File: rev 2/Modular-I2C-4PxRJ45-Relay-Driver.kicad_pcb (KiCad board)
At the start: 2 copper layers, 69.5 x 100 mm, 123 parts, among them J1 Conn_02x03_Odd_Even, J2 Conn_02x03_Odd_Even, J3 Screw_Terminal_01x02, J4 Screw_Terminal_01x02, Q51 2N7002, Q52 2N7002, Q53 2N7002, Q54 2N7002, Q55 2N7002, Q56 2N7002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

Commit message: logo
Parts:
- added G***: LOGO, Vizista_Logo:Vizista-Logo-Text-10mm, F.Cu at (162.7, 34.7)
- added G***: LOGO, Vizista_Logo:Vizista-Logo-Text-20mm, B.Cu at (166.5, 38.5)
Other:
- board text added: "Based on design by Jon Oxer by Austin's Creations"

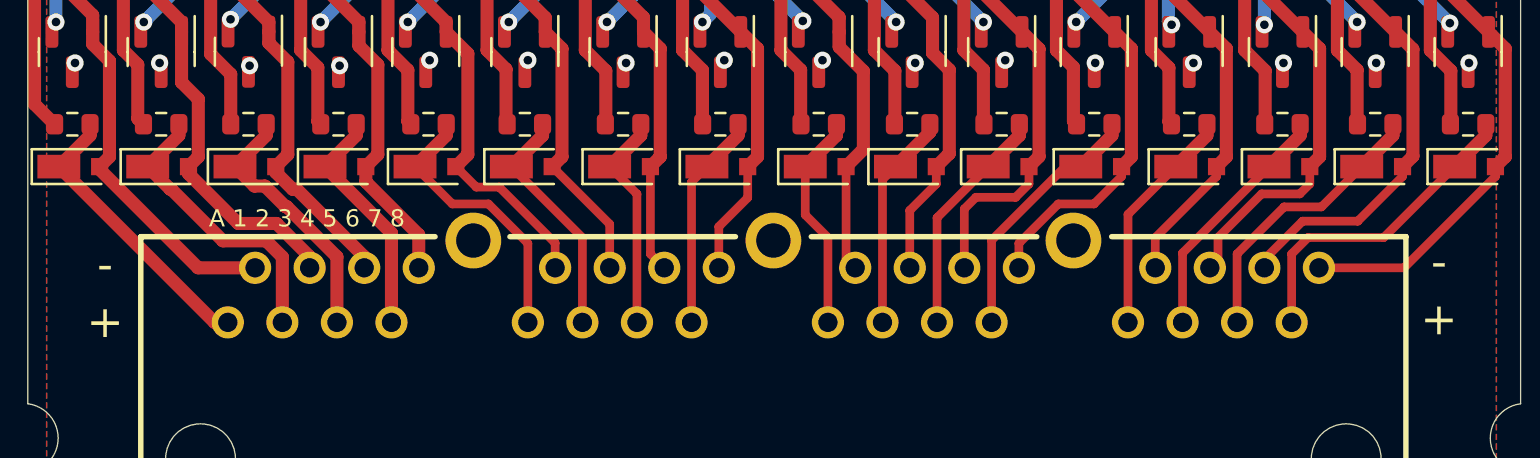
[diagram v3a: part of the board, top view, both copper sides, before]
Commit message: RJ45 to Pluggable break out
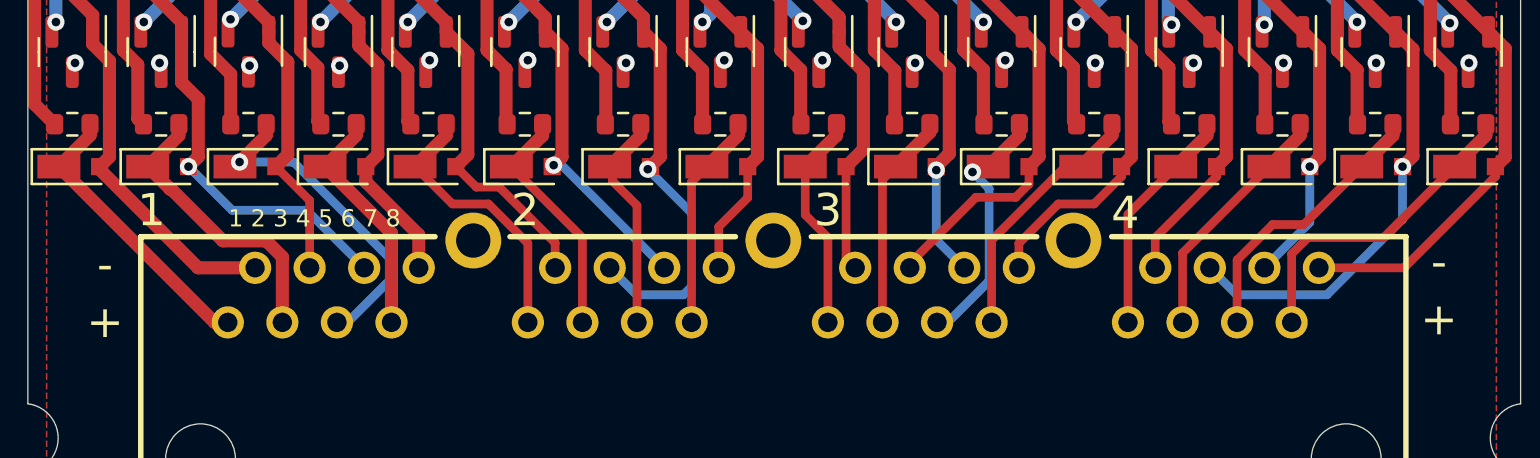
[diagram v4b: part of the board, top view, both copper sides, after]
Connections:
- RJ45-1 pad A4: RC2- -> RC3-
- RJ45-1 pad A6: RC3- -> RC2-
- RJ45-1 pad B4: RC6- -> RC7-
- RJ45-1 pad B6: RC7- -> RC6-
- RJ45-1 pad C4: RC10- -> RC11-
- RJ45-1 pad C6: RC11- -> RC10-
- RJ45-1 pad D4: RC14- -> RC15-
- RJ45-1 pad D6: RC15- -> RC14-
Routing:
- net RC7-: track 14.9 -> 20.9 mm, vias 0 -> 1
- net RC15-: track 18.9 -> 23.4 mm, vias 0 -> 1
- net RC3+: track 12.1 -> 15.8 mm, vias 0 -> 1
- net RC14-: track 17.6 -> 15.6 mm, vias 0 -> 1
- net RC2-: track 18.1 -> 20.1 mm, vias 0 -> 1
- net RC6-: track 15.8 -> 17.1 mm, vias 0 -> 1
- net RC3-: track 16.6 -> 15.4 mm
- net RC11-: track 17.0 -> 18.1 mm
- net RC11+: track 10.8 -> 11.2 mm, vias 0 -> 1
- net RC10-: track 15.2 -> 15.3 mm, vias 0 -> 1
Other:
- board text added: "1 2 3 4 5 6 7 8"
- board text added: "3"
- board text added: "4"
- board text removed: "A 1 2 3 4 5 6 7 8"

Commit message: cleanup
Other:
- board text removed: "1: Data 1 2: Data 2 3: Data 3 4: VIN 5: VIN 6: Data 4 7: GND 8: GND"
- board text removed: "Based on design by Jon Oxer by Austin's Creations modified by Mattar"
- board text removed: "Copyright 2019-2021 SuperHouse Automation Pty Ltd Released under the terms of the TAPR Open Hardware License: www.tapr.org/OHL"
- board text removed: "RJ45 Pinout"
- board text removed: "www.superhouse.tv/i2crj45"
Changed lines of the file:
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@@
       ) (layer "B.SilkS") (width 0) (fill solid))
   )
-  (gr_line (start 348.456014 74.534986) (end 348.456014 89.534986) (layer "B.SilkS") (width 0.254))
-  (gr_arc (start 348.456014 89.534986) (mid 347.870233 90.949214) (end 346.456014 91.534986) (layer "B.SilkS") (width 0.254))
-  (gr_arc (start 333.956014 91.534986) (mid 332.541796 90.949204) (end 331.956014 89.534986) (layer "B.SilkS") (width 0.254))
   (gr_line (start 173.688351 56.1308) (end 170.894351 54.3528) (layer "B.SilkS") (width 0.254))
   (gr_line (start 173.180351 55.8768) (end 172.926351 55.8768) (layer "B.SilkS") (width 0.254))
   (gr_line (start 169.116351 55.8768) (end 170.894351 54.6068) (layer "B.SilkS") (width 0.254))
-  (gr_arc (start 346.456014 72.534986) (mid 347.870223 73.120777) (end 348.456014 74.534986) (layer "B.SilkS") (width 0.254))
   (gr_line (start 168.354351 56.1308) (end 173.688351 56.1308) (layer "B.SilkS") (width 0.254))
   (gr_line (start 170.132351 55.3688) (end 171.402351 55.3688) (layer "B.SilkS") (width 0.4064))
   (gr_line (start 170.894351 54.3528) (end 168.354351 56.1308) (layer "B.SilkS") (width 0.254))
   (gr_line (start 171.402351 55.3688) (end 170.894351 55.1148) (layer "B.SilkS") (width 0.4064))
-  (gr_arc (start 331.956014 74.534986) (mid 332.541806 73.120786) (end 333.956014 72.534986) (layer "B.SilkS") (width 0.254))
-  (gr_line (start 346.451014 91.559986) (end 333.951014 91.559986) (layer "B.SilkS") (width 0.254))
   (gr_line (start 172.418351 55.6228) (end 170.894351 54.8608) (layer "B.SilkS") (width 0.4064))
   (gr_line (start 170.894351 54.6068) (end 172.926351 55.8768) (layer "B.SilkS") (width 0.254))
   (gr_line (start 172.926351 55.8768) (end 169.116351 55.8768) (layer "B.SilkS") (width 0.254))
   (gr_line (start 170.894351 54.8608) (end 170.132351 55.3688) (layer "B.SilkS") (width 0.4064))
-  (gr_line (start 333.956014 72.534986) (end 346.456014 72.534986) (layer "B.SilkS") (width 0.254))
   (gr_line (start 169.624351 55.6228) (end 172.418351 55.6228) (layer "B.SilkS") (width 0.4064))
   (gr_arc (start 126.7449 83.8794) (mid 126.598453 84.232953) (end 126.2449 84.3794) (layer "F.SilkS") (width 0.15))
@@
     (effects (font (size 1.5 1.5) (thickness 0.3)) (justify mirror))
   )
-  (gr_text "www.superhouse.tv/i2crj45" (at 341.757 108.585) (layer "B.SilkS")
-    (effects (font (size 1.909 1.909) (thickness 0.391)) (justify bottom mirror))
-  )
   (gr_text "Based on design \n by Jon Oxer\n by Austin's Creations\n" (at 152.4 52.578) (layer "B.SilkS")
     (effects (font (size 1.180592 1.180592) (thickness 0.241808)) (justify left bottom mirror))
-  )
-  (gr_text "Modular\n4-Port\nI2C RJ45\nRelay Driver Breakout" (at 345.44 52.705) (layer "B.SilkS")
-    (effects (font (size 2.324 2) (thickness 0.476)) (justify left bottom mirror))
   )
   (gr_text "VCC" (at 121.567 47.197 270) (layer "B.SilkS")
@@
     (effects (font (size 0.8 0.8) (thickness 0.2)) (justify mirror))
   )
-  (gr_text "1: Data 1\n2: Data 2\n3: Data 3\n4: VIN\n5: VIN\n6: Data 4\n7: GND\n8: GND" (at 344.773014 90.797986) (layer "B.SilkS")
-    (effects (font (size 1.26 1.26) (thickness 0.24)) (justify left bottom mirror))
-  )
   (gr_text "GND" (at 116.967 52.197 270) (layer "B.SilkS")
     (effects (font (size 0.8 0.8) (thickness 0.2)) (justify mirror))
@@
     (effects (font (size 0.8 0.8) (thickness 0.2)) (justify mirror))
   )
-  (gr_text "RJ45 Pinout" (at 344.773014 74.414986) (layer "B.SilkS")
-    (effects (font (size 1.148 1.148) (thickness 0.252)) (justify left bottom mirror))
-  )
   (gr_text "2" (at 142.113 117.983) (layer "B.SilkS")
     (effects (font (size 1.5 1.5) (thickness 0.3)) (justify mirror))
   )
-  (gr_text "Copyright 2019-2021 SuperHouse Automation Pty Ltd\n\nReleased under the terms of the TAPR\nOpen Hardware License: www.tapr.org/OHL" (at 362.458 103.759) (layer "B.SilkS")
-    (effects (font (size 1.0541 1.0541) (thickness 0.2159)) (justify left bottom mirror))
-  )
-  (gr_text "Based on design \n by Jon Oxer\n by Austin's Creations\n modified by Mattar\n" (at 347.345 30.861) (layer "B.SilkS")
-    (effects (font (size 1.180592 1.180592) (thickness 0.241808)) (justify left bottom mirror))
-  )
   (gr_text "SCL" (at 121.667 57.097 270) (layer "B.SilkS")

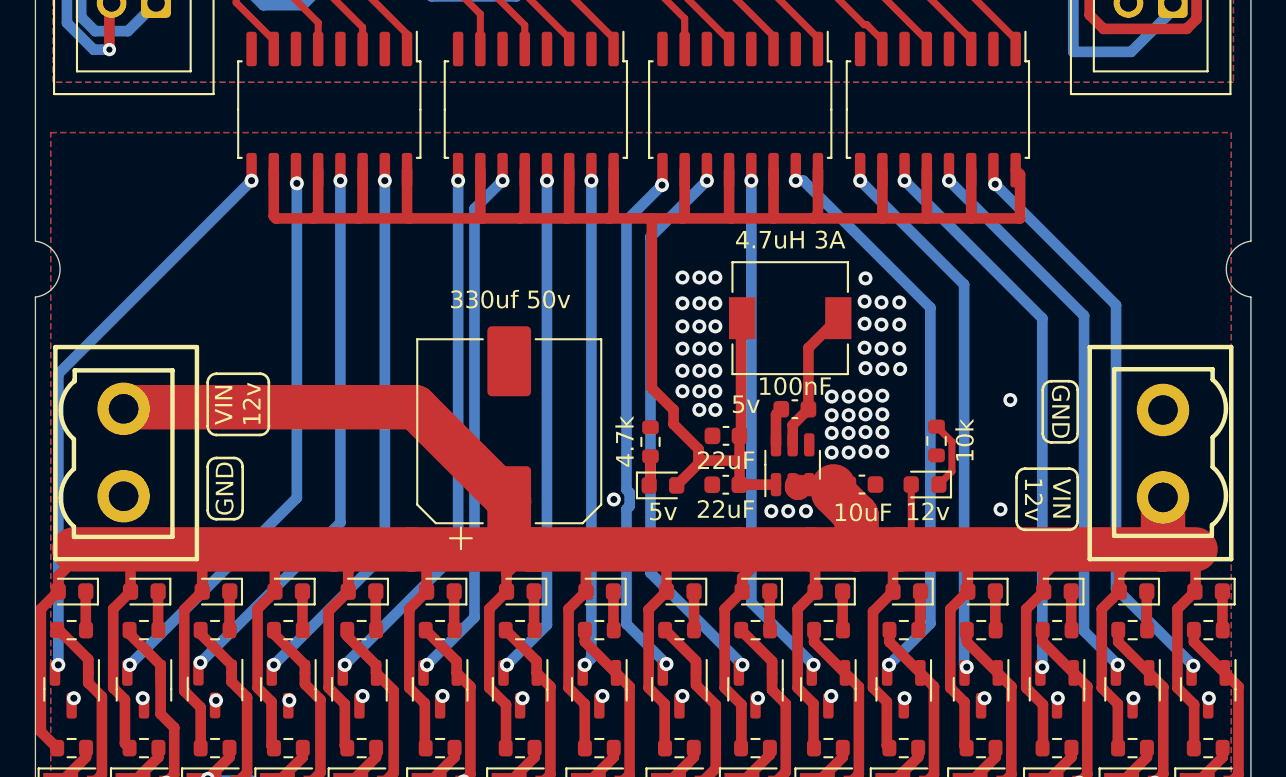
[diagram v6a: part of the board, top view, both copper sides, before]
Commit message: updated to support 5V output for fan speed control in rev2
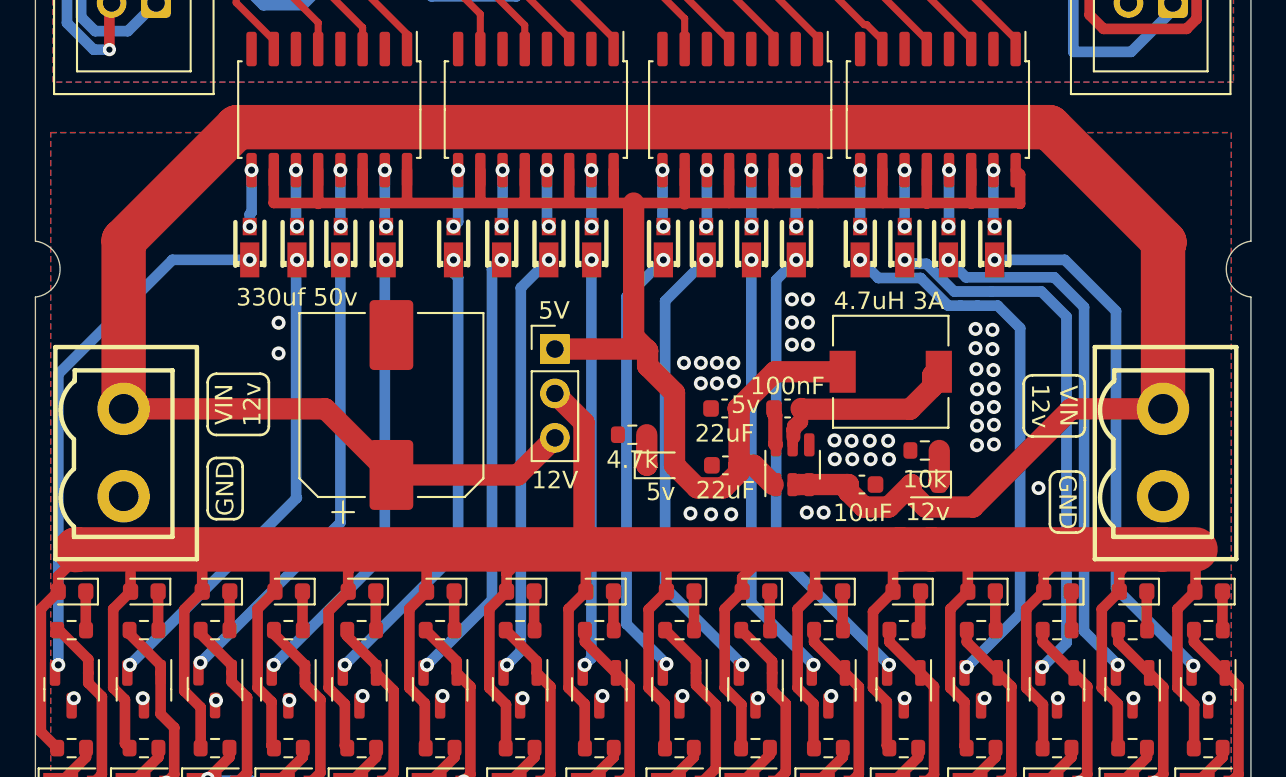
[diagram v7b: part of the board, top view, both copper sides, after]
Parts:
- added D67: 1N4004 SMB, LCSC:LCSC-C94470-MICROSMP_L2.2-W1.3-LS2.5-RD, F.Cu at (134.9, 68.6)
- added D68: 1N4004 SMB, LCSC:LCSC-C94470-MICROSMP_L2.2-W1.3-LS2.5-RD, F.Cu at (132.3, 68.6)
- added D69: 1N4004 SMB, LCSC:LCSC-C94470-MICROSMP_L2.2-W1.3-LS2.5-RD, F.Cu at (129.8, 68.6)
- added D70: 1N4004 SMB, LCSC:LCSC-C94470-MICROSMP_L2.2-W1.3-LS2.5-RD, F.Cu at (127.2, 68.6)
- added D71: 1N4004 SMB, LCSC:LCSC-C94470-MICROSMP_L2.2-W1.3-LS2.5-RD, F.Cu at (138.8, 68.6)
- added D72: 1N4004 SMB, LCSC:LCSC-C94470-MICROSMP_L2.2-W1.3-LS2.5-RD, F.Cu at (141.6, 68.6)
- added D73: 1N4004 SMB, LCSC:LCSC-C94470-MICROSMP_L2.2-W1.3-LS2.5-RD, F.Cu at (144.2, 68.6)
- added D74: 1N4004 SMB, LCSC:LCSC-C94470-MICROSMP_L2.2-W1.3-LS2.5-RD, F.Cu at (146.7, 68.6)
- added D75: 1N4004 SMB, LCSC:LCSC-C94470-MICROSMP_L2.2-W1.3-LS2.5-RD, F.Cu at (150.8, 68.6)
- added D76: 1N4004 SMB, LCSC:LCSC-C94470-MICROSMP_L2.2-W1.3-LS2.5-RD, F.Cu at (153.2, 68.6)
- added D77: 1N4004 SMB, LCSC:LCSC-C94470-MICROSMP_L2.2-W1.3-LS2.5-RD, F.Cu at (155.8, 68.6)
- added D78: 1N4004 SMB, LCSC:LCSC-C94470-MICROSMP_L2.2-W1.3-LS2.5-RD, F.Cu at (158.4, 68.6)
- added D79: 1N4004 SMB, LCSC:LCSC-C94470-MICROSMP_L2.2-W1.3-LS2.5-RD, F.Cu at (162.1, 68.6)
- added D80: 1N4004 SMB, LCSC:LCSC-C94470-MICROSMP_L2.2-W1.3-LS2.5-RD, F.Cu at (164.6, 68.6)
- added D81: 1N4004 SMB, LCSC:LCSC-C94470-MICROSMP_L2.2-W1.3-LS2.5-RD, F.Cu at (167.1, 68.6)
- added D82: 1N4004 SMB, LCSC:LCSC-C94470-MICROSMP_L2.2-W1.3-LS2.5-RD, F.Cu at (169.7, 68.6)
- added JP1: Jumper_3_Open, Connector_PinHeader_2.54mm:PinHeader_1x03_P2.54mm_Vertical, F.Cu at (144.6, 74.7)
- moved C5 6.90 mm to (135.2, 77.8)
- moved L1 6.51 mm to (163.8, 76.0)
- moved C7 1.57 mm to (154.3, 78.0)
- moved D2 1.16 mm to (150.7, 81.3)
- moved R1 1.12 mm to (149.0, 79.5), turned to 0 degrees
- moved C8 1.11 mm to (154.3, 81.3)
- moved R5 0.86 mm to (165.8, 80.5), turned to 180 degrees
- moved C6 0.42 mm to (157.9, 78.0)
- moved J4 0.07 mm to (179.4, 80.6), turned to -90 degrees
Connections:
- LED51 pad 2: VDD -> ADJV
- LED52 pad 2: VDD -> ADJV
- LED53 pad 2: VDD -> ADJV
- LED54 pad 2: VDD -> ADJV
- LED55 pad 2: VDD -> ADJV
- LED56 pad 2: VDD -> ADJV
- LED57 pad 2: VDD -> ADJV
- LED58 pad 2: VDD -> ADJV
- LED59 pad 2: VDD -> ADJV
- LED60 pad 2: VDD -> ADJV
- LED61 pad 2: VDD -> ADJV
- LED62 pad 2: VDD -> ADJV
- LED63 pad 2: VDD -> ADJV
- LED64 pad 2: VDD -> ADJV
- LED65 pad 2: VDD -> ADJV
- LED66 pad 2: VDD -> ADJV
- TH51 pad 1: VDD -> ADJV
- TH52 pad 1: VDD -> ADJV
- TH53 pad 1: VDD -> ADJV
- TH54 pad 1: VDD -> ADJV
- TH55 pad 1: VDD -> ADJV
- TH56 pad 1: VDD -> ADJV
- TH57 pad 1: VDD -> ADJV
- TH58 pad 1: VDD -> ADJV
- TH59 pad 1: VDD -> ADJV
- TH60 pad 1: VDD -> ADJV
- TH61 pad 1: VDD -> ADJV
- TH62 pad 1: VDD -> ADJV
- TH63 pad 1: VDD -> ADJV
- TH64 pad 1: VDD -> ADJV
- TH65 pad 1: VDD -> ADJV
- TH66 pad 1: VDD -> ADJV
- U3 pad 11: p1-b5 -> Net-(D69-A)
- U3 pad 13: p1-c5 -> Net-(D68-A)
- U3 pad 15: p1-d5 -> Net-(D67-A)
- U3 pad 9: p1-a5 -> Net-(D70-A)
- U4 pad 11: p2-b5 -> Net-(D72-A)
- U4 pad 13: p2-c5 -> Net-(D73-A)
- U4 pad 15: p2-d5 -> Net-(D74-A)
- U4 pad 9: p2-a5 -> Net-(D71-A)
- U5 pad 11: p3-b5 -> Net-(D76-A)
- U5 pad 13: p3-c5 -> Net-(D77-A)
- U5 pad 15: p3-d5 -> Net-(D78-A)
- U5 pad 9: p3-a5 -> Net-(D75-A)
- U6 pad 11: p4-b5 -> Net-(D80-A)
- U6 pad 13: p4-c5 -> Net-(D81-A)
- U6 pad 15: p4-d5 -> Net-(D82-A)
- U6 pad 9: p4-a5 -> Net-(D79-A)
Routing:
- net ADJV: track 0.00 -> 252.1 mm
- net VDD: track 281.5 -> 136.5 mm
- net +5V: track 118.7 -> 111.5 mm
- net p3-d5: track 32.1 -> 26.3 mm
- net p3-b5: track 31.2 -> 26.0 mm
- net Net-(U2-SW): track 8.33 -> 13.3 mm
- net p2-b5: track 29.5 -> 24.9 mm
- net p3-c5: track 29.2 -> 24.6 mm
- net p2-d5: track 27.8 -> 23.3 mm
- net p1-c5: track 30.9 -> 26.4 mm
- net p1-d5: track 30.3 -> 25.8 mm
- net p2-c5: track 28.6 -> 24.1 mm
- net p2-a5: track 30.4 -> 25.9 mm
- net p3-a5: track 29.3 -> 24.9 mm
- net p1-b5: track 31.5 -> 27.2 mm
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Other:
- board text added: "12V"
- board text added: "5V"
- board text added: "Modular 4-Port I2C RJ45 Relay Driver"
- board text removed: "Modular 4-Port I2C RJ45 Relay Driver Breakout"

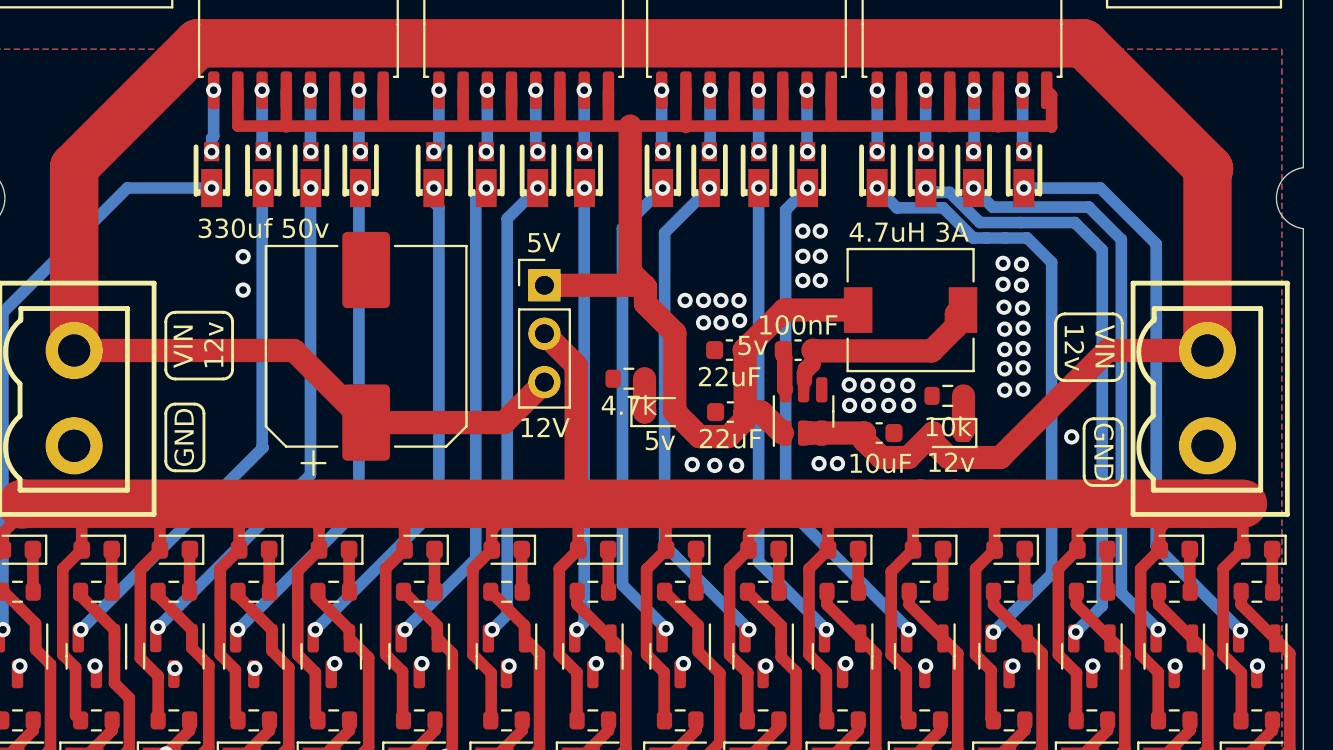
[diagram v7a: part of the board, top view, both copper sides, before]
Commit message: 5V input suport
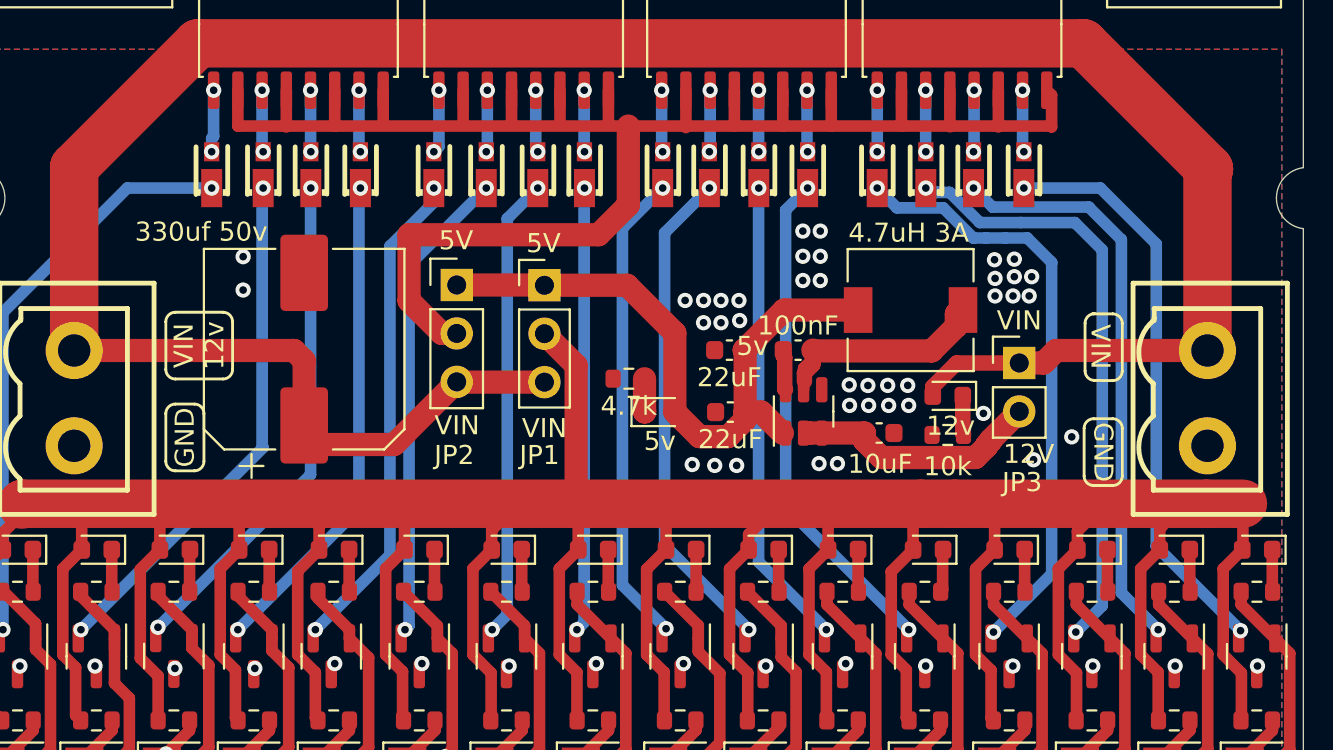
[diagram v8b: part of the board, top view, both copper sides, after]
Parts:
- added JP2: Jumper_3_Open, Connector_PinHeader_2.54mm:PinHeader_1x03_P2.54mm_Vertical, F.Cu at (140.0, 74.6)
- added JP3: Jumper_2_Small_Open, Connector_PinHeader_2.54mm:PinHeader_1x02_P2.54mm_Vertical, F.Cu at (169.5, 78.7)
- moved C5 3.25 mm to (132.0, 78.0)
- moved R5 2.05 mm to (165.8, 82.5)
- moved D3 1.95 mm to (165.8, 80.5)
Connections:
- C9 pad 2: VDD -> 12VIN
- U2 pad 2: VDD -> 12VIN
- U2 pad 3: VDD -> 12VIN
- U3 pad 10: +5V -> OptoIN
- U3 pad 12: +5V -> OptoIN
- U3 pad 14: +5V -> OptoIN
- U3 pad 16: +5V -> OptoIN
- U4 pad 10: +5V -> OptoIN
- U4 pad 12: +5V -> OptoIN
- U4 pad 14: +5V -> OptoIN
- U4 pad 16: +5V -> OptoIN
- U5 pad 10: +5V -> OptoIN
- U5 pad 12: +5V -> OptoIN
- U5 pad 14: +5V -> OptoIN
- U5 pad 16: +5V -> OptoIN
- U6 pad 10: +5V -> OptoIN
- U6 pad 12: +5V -> OptoIN
- U6 pad 14: +5V -> OptoIN
- U6 pad 16: +5V -> OptoIN
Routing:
- net OptoIN: track 0.00 -> 95.6 mm
- net +5V: track 111.5 -> 34.2 mm
- net 12VIN: track 0.00 -> 12.8 mm
- net VDD: track 136.5 -> 129.8 mm
- net GNDPWR: vias 59 -> 55
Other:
- board text added: "JP1"
- board text added: "JP2"
- board text added: "JP3"
- board text added: "VIN"
